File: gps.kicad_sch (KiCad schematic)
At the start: 6 parts, among them J16 Conn_Coaxial, U17 MAX-M8Q

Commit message: working on v2
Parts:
- removed R42: 10K, Resistor_SMD:R_0603_1608Metric, symbol Device:R
- added TP?: GPS_RESET, symbol Connector:TestPoint
- U17: value MAX-M8Q -> MAX-M10S
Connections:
- net at U17.9 (~{RESET}): now also TP?.1
- no-connect marks 4 -> 5
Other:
- note added: "5% or lower"
- moved on the sheet: C29, J16, L2, R43

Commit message: v2 time
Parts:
- C49: renamed from C29; footprint Capacitor_SMD:C_0603_1608Metric -> Capacitor_SMD:C_0402_1005Metric
- L4: renamed from L2; footprint Inductor_SMD:L_0603_1608Metric -> Inductor_SMD:L_0402_1005Metric; Part (none) -> LQG15HZ27NH02D
- TP15: renamed from TP?; footprint (none) -> TestPoint:TestPoint_Pad_D1.0mm
- renumbered J16 to J10, R43 to R30, U17 to U19
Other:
- note added: "10ohm, 5%, 0.25W"
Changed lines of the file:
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@@
+    (effects (font (size 1.27 1.27)) (justify left bottom))
+  )
+  (text "10ohm, 5%, 0.25W" (at 134.62 64.77 0)
     (effects (font (size 1.27 1.27)) (justify left bottom))
   )
@@
   (symbol (lib_id "Connector:Conn_Coaxial") (at 156.21 52.07 90) (unit 1)
     (in_bom yes) (on_board yes)
-    (property "Reference" "J16" (id 0) (at 158.0134 46.0502 90))
+    (property "Reference" "J10" (id 0) (at 158.0134 46.0502 90))
     (property "Value" "Conn_Coaxial" (id 1) (at 158.0134 48.3616 90))
     (property "Footprint" "Connector_Coaxial:SMA_Molex_73251-1153_EdgeMount_Horizontal" (id 2) (at 156.21 52.07 0)
@@
   (symbol (lib_id "power:GND") (at 139.7 119.38 0) (unit 1)
     (in_bom yes) (on_board yes)
-    (property "Reference" "#PWR0107" (id 0) (at 139.7 125.73 0)
+    (property "Reference" "#PWR0119" (id 0) (at 139.7 125.73 0)
       (effects (font (size 1.27 1.27)) hide)
     )
@@
   (symbol (lib_id "Connector:TestPoint") (at 118.11 106.68 90) (unit 1)
     (in_bom yes) (on_board yes) (fields_autoplaced)
-    (property "Reference" "TP?" (id 0) (at 114.808 100.33 90))
+    (property "Reference" "TP15" (id 0) (at 114.808 100.33 90))
     (property "Value" "GPS_RESET" (id 1) (at 114.808 102.87 90))
-    (property "Footprint" "" (id 2) (at 118.11 101.6 0)
+    (property "Footprint" "TestPoint:TestPoint_Pad_D1.0mm" (id 2) (at 118.11 101.6 0)
       (effects (font (size 1.27 1.27)) hide)
     )
@@
   (symbol (lib_id "power:+3V3") (at 134.62 72.39 0) (unit 1)
     (in_bom yes) (on_board yes)
-    (property "Reference" "#PWR0106" (id 0) (at 134.62 76.2 0)
+    (property "Reference" "#PWR0118" (id 0) (at 134.62 76.2 0)
       (effects (font (size 1.27 1.27)) hide)
     )
@@
   (symbol (lib_id "pspice:INDUCTOR") (at 156.21 67.31 90) (unit 1)
     (in_bom yes) (on_board yes)
-    (property "Reference" "L2" (id 0) (at 157.3276 66.1416 90)
+    (property "Reference" "L4" (id 0) (at 157.3276 66.1416 90)
       (effects (font (size 1.27 1.27)) (justify right))
     )
@@
       (effects (font (size 1.27 1.27)) (justify right))
     )
-    (property "Footprint" "Inductor_SMD:L_0603_1608Metric" (id 2) (at 156.21 67.31 0)
+    (property "Footprint" "Inductor_SMD:L_0402_1005Metric" (id 2) (at 156.21 67.31 0)
       (effects (font (size 1.27 1.27)) hide)
     )
     (property "Datasheet" "~" (id 3) (at 156.21 67.31 0)
+      (effects (font (size 1.27 1.27)) hide)
+    )
+    (property "Part" "LQG15HZ27NH02D" (id 4) (at 156.21 67.31 90)
       (effects (font (size 1.27 1.27)) hide)
     )
@@
   (symbol (lib_id "Device:R") (at 148.59 76.2 270) (unit 1)
     (in_bom yes) (on_board yes)
-    (property "Reference" "R43" (id 0) (at 148.59 70.9422 90))
+    (property "Reference" "R30" (id 0) (at 148.59 70.9422 90))
     (property "Value" "10" (id 1) (at 148.59 73.2536 90))
     (property "Footprint" "Resistor_SMD:R_0603_1608Metric" (id 2) (at 148.59 74.422 90)
@@
   (symbol (lib_id "Device:C") (at 161.29 80.01 0) (unit 1)
     (in_bom yes) (on_board yes)
-    (property "Reference" "C29" (id 0) (at 164.211 78.8416 0)
+    (property "Reference" "C49" (id 0) (at 164.211 78.8416 0)
       (effects (font (size 1.27 1.27)) (justify left))
     )
@@
       (effects (font (size 1.27 1.27)) (justify left))
     )
-    (property "Footprint" "Capacitor_SMD:C_0603_1608Metric" (id 2) (at 162.2552 83.82 0)
+    (property "Footprint" "Capacitor_SMD:C_0402_1005Metric" (id 2) (at 162.2552 83.82 0)
       (effects (font (size 1.27 1.27)) hide)
     )
@@
   (symbol (lib_id "RF_GPS:MAX-M8Q") (at 139.7 96.52 0) (unit 1)
     (in_bom yes) (on_board yes)
-    (property "Reference" "U17" (id 0) (at 149.86 80.01 0))
+    (property "Reference" "U19" (id 0) (at 149.86 80.01 0))
     (property "Value" "MAX-M10S" (id 1) (at 146.05 113.03 0))
     (property "Footprint" "RF_GPS:ublox_MAX" (id 2) (at 149.86 113.03 0)
@@
   (symbol (lib_id "power:GND") (at 161.29 86.36 0) (unit 1)
     (in_bom yes) (on_board yes)
-    (property "Reference" "#PWR0108" (id 0) (at 161.29 92.71 0)
+    (property "Reference" "#PWR0120" (id 0) (at 161.29 92.71 0)
       (effects (font (size 1.27 1.27)) hide)
     )

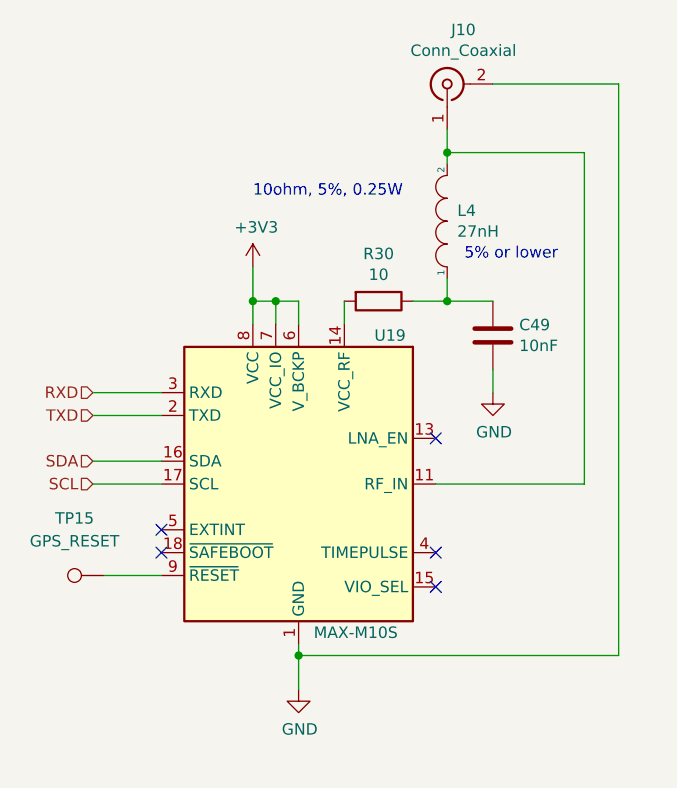
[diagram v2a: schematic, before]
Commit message: changed bb and power side
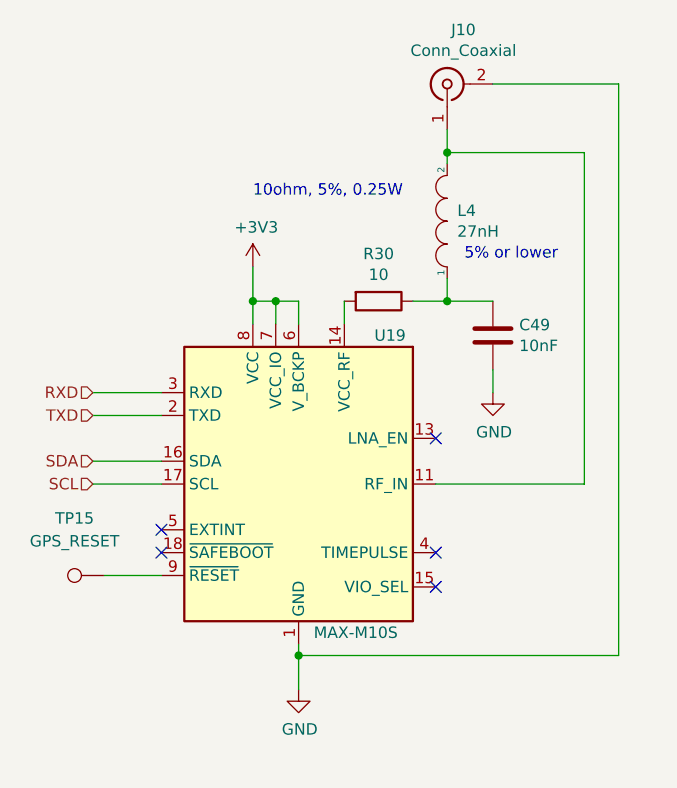
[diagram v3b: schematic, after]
